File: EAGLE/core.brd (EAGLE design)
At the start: 20.3 x 33 mm, 46 parts, among them Q1 MMDT3904, U1 MIC5219, U3 STM32F10XCXT6, U4 SST25VF040B-50-4I-S2AF, X1 USBUSB-MICROB-ALIGN, Y1 8Mhz

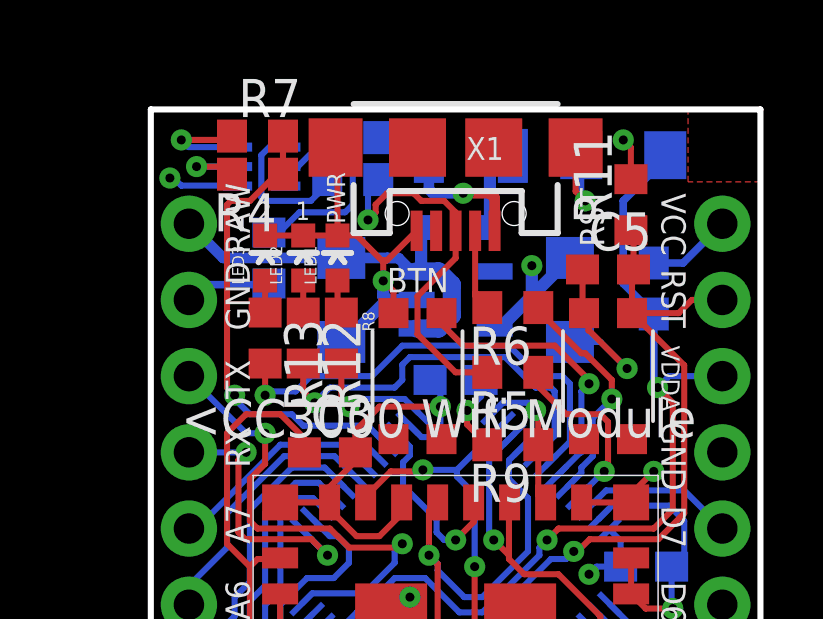
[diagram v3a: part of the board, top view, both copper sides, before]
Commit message: Renumbered parts
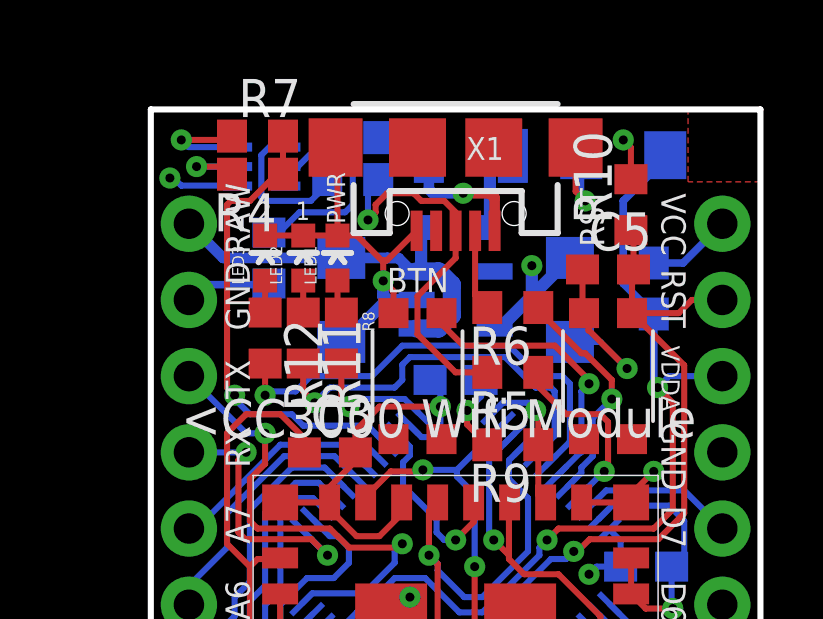
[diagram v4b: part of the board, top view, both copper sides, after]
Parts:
- removed R14: 1K, rcl:R0603
- added R10: 10K, rcl:R0603
- R11: value 10K -> 1K
- moved R13 18.7 mm to (9.65, 7.62), flipped to the bottom
- moved R11 11.8 mm to (5.08, 25.4), turned to 270 degrees
- moved R12 1.27 mm to (3.81, 25.4)
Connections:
- net !RST: now also R10.1; no longer R11.1
- net +3V3: now also R10.2, R13.2; no longer R11.2, R14.2
- net LED1: now also R11.2; no longer R12.2
- net LED2: now also R12.2; no longer R13.2
- net MEM_CS: now also R13.1; no longer R14.1
- net N$10: now also R12.1; no longer R13.1
- net N$2: now also R11.1; no longer R12.1
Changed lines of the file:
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@@
 </element>
 <element name="RESET" library="okie" package="PUSHBUTTON-KMR241GLFS" value="KMR211GLFS" x="15.24" y="24.13" smashed="yes" rot="R90"/>
-<element name="R11" library="rcl" package="R0603" value="10K" x="16.002" y="29.845" smashed="yes" rot="R90">
+<element name="R10" library="rcl" package="R0603" value="10K" x="16.002" y="29.845" smashed="yes" rot="R90">
 <attribute name="NAME" x="15.367" y="29.21" size="1.27" layer="25" rot="R90"/>
 <attribute name="VALUE" x="15.494" y="31.369" size="0.6096" layer="27"/>
 </element>
 <element name="BTN" library="okie" package="PUSHBUTTON-KMR241GLFS" value="KMR211GLFS" x="8.89" y="24.13" smashed="yes" rot="R90"/>
-<element name="R13" library="rcl" package="R0603" value="1K" x="3.81" y="25.4" smashed="yes" rot="R270">
+<element name="R12" library="rcl" package="R0603" value="1K" x="3.81" y="25.4" smashed="yes" rot="R270">
 <attribute name="NAME" x="4.445" y="26.035" size="1.27" layer="25" rot="R270"/>
 <attribute name="VALUE" x="3.302" y="23.368" size="0.6096" layer="27"/>
@@
 <attribute name="VALUE" x="5.9055" y="28.448" size="0.4064" layer="27" rot="R90"/>
 </element>
-<element name="R12" library="rcl" package="R0603" value="1K" x="5.08" y="25.4" smashed="yes" rot="R270">
+<element name="R11" library="rcl" package="R0603" value="1K" x="5.08" y="25.4" smashed="yes" rot="R270">
 <attribute name="NAME" x="5.715" y="26.035" size="1.27" layer="25" rot="R270"/>
 <attribute name="VALUE" x="4.572" y="23.368" size="0.6096" layer="27"/>
@@
 </element>
 <element name="Q1" library="SparkFun-DiscreteSemi" package="SOT363" value="MMDT3904" x="3.683" y="31.115" smashed="yes" rot="MR90"/>
-<element name="R14" library="rcl" package="R0603" value="1K" x="9.652" y="7.62" smashed="yes" rot="MR270">
+<element name="R13" library="rcl" package="R0603" value="1K" x="9.652" y="7.62" smashed="yes" rot="MR270">
 <attribute name="NAME" x="9.017" y="8.255" size="1.27" layer="26" rot="MR270"/>
 <attribute name="VALUE" x="10.16" y="9.144" size="0.6096" layer="28" rot="MR0"/>
@@
 <contactref element="R8" pad="2"/>
 <contactref element="C2" pad="A"/>
-<contactref element="R11" pad="2"/>
+<contactref element="R10" pad="2"/>
 <contactref element="U4" pad="8"/>
 <contactref element="JP2" pad="1"/>
@@
 <contactref element="C7" pad="1"/>
 <contactref element="Q1" pad="3"/>
-<contactref element="R14" pad="2"/>
+<contactref element="R13" pad="2"/>
 <polygon width="0.2032" layer="15" isolate="0.2032">
 <vertex x="0" y="33.02"/>
@@
 <contactref element="U3" pad="7"/>
 <contactref element="RESET" pad="P$2"/>
-<contactref element="R11" pad="1"/>
+<contactref element="R10" pad="1"/>
 <contactref element="JP2" pad="2"/>
 <wire x1="18.034" y1="26.67" x2="19.05" y2="26.67" width="0.2032" layer="1"/>
@@
 </signal>
 <signal name="N$2">
-<contactref element="R12" pad="1"/>
+<contactref element="R11" pad="1"/>
 <contactref element="LED2" pad="A"/>
 <wire x1="5.08" y1="26.25" x2="5.08" y2="27.317" width="0.2032" layer="1"/>
 </signal>
 <signal name="N$10">
-<contactref element="R13" pad="1"/>
+<contactref element="R12" pad="1"/>
 <contactref element="LED3" pad="A"/>
 <wire x1="3.81" y1="26.25" x2="3.81" y2="27.317" width="0.2032" layer="1"/>
@@
 <contactref element="U4" pad="1"/>
 <contactref element="U3" pad="46"/>
-<contactref element="R14" pad="1"/>
+<contactref element="R13" pad="1"/>
 <wire x1="11.303" y1="10.2616" x2="11.303" y2="9.271" width="0.2032" layer="16"/>
 <wire x1="11.303" y1="9.271" x2="10.502" y2="8.47" width="0.2032" layer="16"/>
@@
 <signal name="LED1">
 <contactref element="U3" pad="29"/>
-<contactref element="R12" pad="2"/>
+<contactref element="R11" pad="2"/>
 <wire x1="12.811653125" y1="21.492309375" x2="13.462" y2="22.14265625" width="0.2032" layer="16"/>
 <wire x1="13.462" y1="22.14265625" x2="13.462" y2="23.622" width="0.2032" layer="16"/>
@@
 <signal name="LED2">
 <contactref element="U3" pad="30"/>
-<contactref element="R13" pad="2"/>
+<contactref element="R12" pad="2"/>
 <wire x1="7.366" y1="24.13" x2="5.334" y2="24.13" width="0.2032" layer="16"/>
 <wire x1="13.16520625" y1="21.13875625" x2="13.97" y2="21.94355" width="0.2032" layer="16"/>

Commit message: Updated assembly sheets to v0.1.0
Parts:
- X1: value USBUSB-MICROB-ALIGN -> USB-MICROB
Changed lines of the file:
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@@
 <setting verticaltext="up"/>
 </settings>
-<grid distance="5" unitdist="mil" unit="mil" style="lines" multiple="1" display="yes" altdistance="0.005" altunitdist="inch" altunit="inch"/>
+<grid distance="0.001" unitdist="inch" unit="inch" style="lines" multiple="1" display="yes" altdistance="0.005" altunitdist="inch" altunit="inch"/>
 <layers>
-<layer number="1" name="Top" color="4" fill="1" visible="yes" active="yes"/>
+<layer number="1" name="Top" color="4" fill="1" visible="no" active="yes"/>
 <layer number="2" name="$GND" color="13" fill="1" visible="no" active="yes"/>
 <layer number="3" name="Route3" color="4" fill="3" visible="no" active="no"/>
@@
 <layer number="14" name="Route14" color="1" fill="6" visible="no" active="no"/>
 <layer number="15" name="$+3V3" color="11" fill="1" visible="no" active="yes"/>
-<layer number="16" name="Bottom" color="1" fill="1" visible="yes" active="yes"/>
+<layer number="16" name="Bottom" color="1" fill="1" visible="no" active="yes"/>
 <layer number="17" name="Pads" color="2" fill="1" visible="yes" active="yes"/>
-<layer number="18" name="Vias" color="2" fill="1" visible="yes" active="yes"/>
-<layer number="19" name="Unrouted" color="6" fill="1" visible="yes" active="yes"/>
+<layer number="18" name="Vias" color="2" fill="1" visible="no" active="yes"/>
+<layer number="19" name="Unrouted" color="6" fill="1" visible="no" active="yes"/>
 <layer number="20" name="Dimension" color="6" fill="1" visible="yes" active="yes"/>
 <layer number="21" name="tPlace" color="16" fill="1" visible="no" active="yes"/>
 <layer number="22" name="bPlace" color="14" fill="1" visible="yes" active="yes"/>
-<layer number="23" name="tOrigins" color="15" fill="1" visible="yes" active="yes"/>
+<layer number="23" name="tOrigins" color="15" fill="1" visible="no" active="yes"/>
 <layer number="24" name="bOrigins" color="15" fill="1" visible="yes" active="yes"/>
 <layer number="25" name="tNames" color="7" fill="1" visible="no" active="yes"/>
 <layer number="26" name="bNames" color="7" fill="1" visible="no" active="yes"/>
 <layer number="27" name="tValues" color="7" fill="1" visible="no" active="yes"/>
-<layer number="28" name="bValues" color="7" fill="1" visible="no" active="yes"/>
+<layer number="28" name="bValues" color="7" fill="1" visible="yes" active="yes"/>
 <layer number="29" name="tStop" color="7" fill="3" visible="no" active="yes"/>
 <layer number="30" name="bStop" color="7" fill="6" visible="no" active="yes"/>
 <layer number="31" name="tCream" color="7" fill="4" visible="no" active="yes"/>
-<layer number="32" name="bCream" color="7" fill="5" visible="no" active="yes"/>
+<layer number="32" name="bCream" color="7" fill="5" visible="yes" active="yes"/>
 <layer number="33" name="tFinish" color="6" fill="3" visible="no" active="yes"/>
 <layer number="34" name="bFinish" color="6" fill="6" visible="no" active="yes"/>
@@
 <layer number="49" name="Reference" color="7" fill="1" visible="no" active="yes"/>
 <layer number="50" name="dxf" color="7" fill="1" visible="no" active="yes"/>
-<layer number="51" name="tDocu" color="6" fill="1" visible="yes" active="yes"/>
-<layer number="52" name="bDocu" color="7" fill="1" visible="no" active="yes"/>
+<layer number="51" name="tDocu" color="6" fill="1" visible="no" active="yes"/>
+<layer number="52" name="bDocu" color="7" fill="1" visible="yes" active="yes"/>
 <layer number="53" name="tGND_GNDA" color="7" fill="9" visible="no" active="no"/>
 <layer number="54" name="bGND_GNDA" color="1" fill="9" visible="no" active="no"/>
@@
 <attribute name="VALUE" x="11.557" y="27.051" size="0.6096" layer="27"/>
 </element>
-<element name="X1" library="Spark" package="USB-MICROB-ALIGN" value="USBUSB-MICROB-ALIGN" x="10.16" y="31.75" smashed="yes" rot="R180">
+<element name="X1" library="Spark" package="USB-MICROB-ALIGN" value="USB-MICROB" x="10.16" y="31.75" smashed="yes" rot="R180">
 <attribute name="NAME" x="11.76" y="32.1" size="0.762" layer="25" rot="R180"/>
-<attribute name="VALUE" x="7.62" y="34.671" size="0.6096" layer="27"/>
+<attribute name="VALUE" x="7.366" y="34.671" size="0.6096" layer="27"/>
 </element>
 <element name="F1" library="SparkFun" package="PTC-1206" value="500mA" x="10.668" y="31.4706" smashed="yes" rot="MR180">
@@
 <element name="R1" library="rcl" package="R0603" value="10K" x="6.731" y="32.0802" smashed="yes" rot="MR180">
 <attribute name="NAME" x="6.096" y="31.4452" size="1.27" layer="26" rot="MR180"/>
-<attribute name="VALUE" x="7.239" y="31.0642" size="0.4064" layer="28" rot="MR0"/>
+<attribute name="VALUE" x="7.2644" y="31.2166" size="0.4064" layer="28" rot="MR0"/>
 </element>
 <element name="R3" library="rcl" package="R0603" value="1K5" x="6.731" y="30.6832" smashed="yes" rot="MR0">
 <attribute name="NAME" x="7.366" y="31.3182" size="1.27" layer="26" rot="MR0"/>
-<attribute name="VALUE" x="7.239" y="31.3182" size="0.4064" layer="28" rot="MR0"/>
+<attribute name="VALUE" x="7.1882" y="29.6418" size="0.4064" layer="28" rot="MR0"/>
 </element>
 <element name="C7" library="rcl" package="C0603" value="100nF" x="10.16" y="24.003" smashed="yes" rot="MR0">
@@
 <element name="L2" library="SparkFun-Passives" package="0603" value="Bead" x="16.764" y="27.051" smashed="yes" rot="MR270">
 <attribute name="NAME" x="16.002" y="27.94" size="0.4064" layer="26" font="vector" rot="MR270"/>
-<attribute name="VALUE" x="17.526" y="25.146" size="0.4064" layer="28" font="vector" rot="MR0"/>
+<attribute name="VALUE" x="17.4498" y="25.146" size="0.4064" layer="28" font="vector" rot="MR0"/>
 </element>
 <element name="R4" library="rcl" package="R0603" value="1K" x="3.556" y="30.861" smashed="yes" rot="R180">
@@
 </signal>
 </signals>
-<errors>
-</errors>
 </board>
 </drawing>

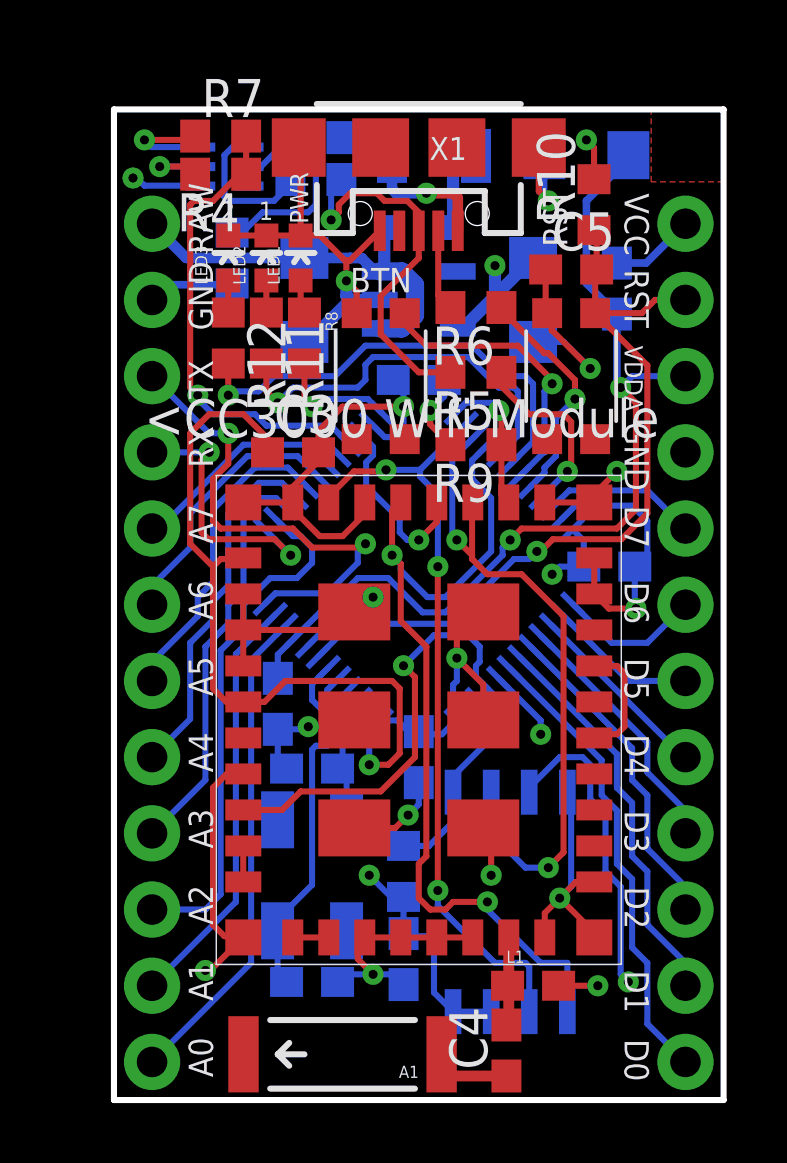
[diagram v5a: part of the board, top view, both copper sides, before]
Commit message: WIP for Issue #5, #7, #8, #9
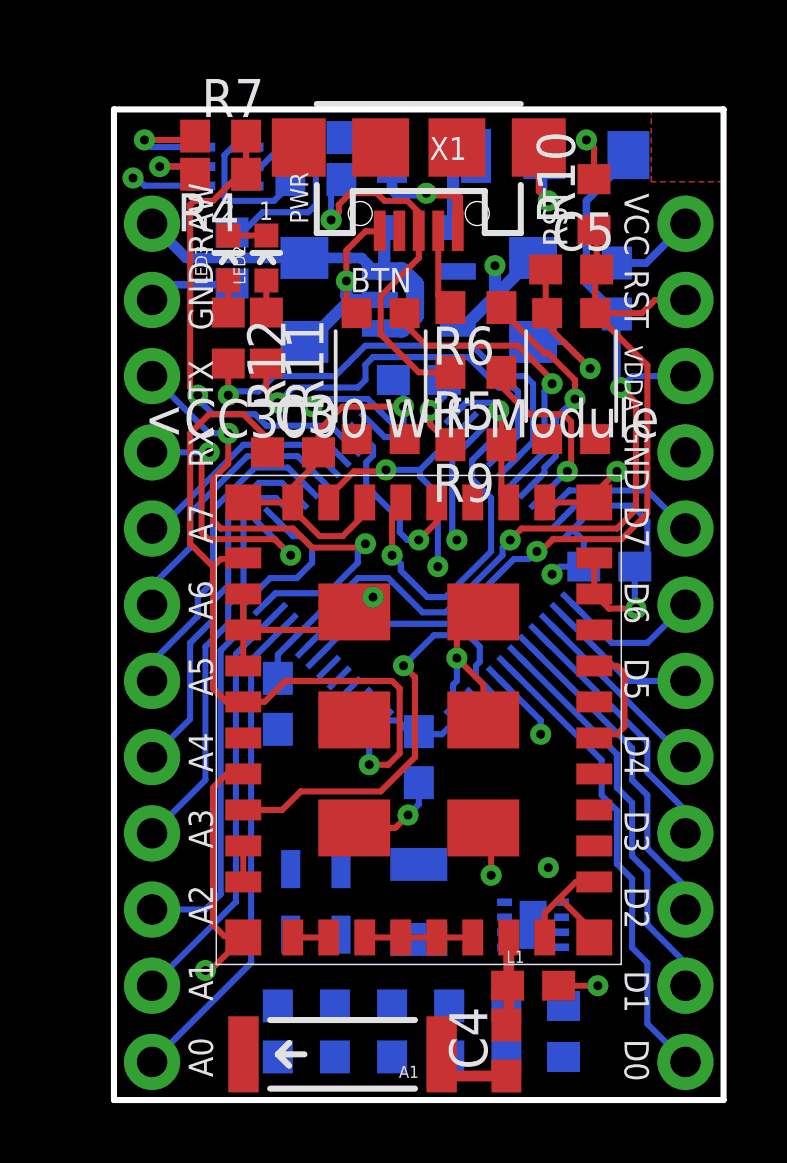
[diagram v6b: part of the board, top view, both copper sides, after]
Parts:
- removed LED1: Red, SparkFun:LED-0603
- removed R8: 1K, rcl:R0603
- added C14, C15: 12.5pF, rcl:C0603
- added Y2: 32Khz, Spark:FC135
- U4: value SST25VF040B-50-4I-S2AF -> SST25VF040B-Q; device Silicon_Storage_Tech_By_element14_Batch_1:SOIC127P790X216-8N -> Spark:WSON-8-PAD
- Y1: device SparkFun:CRYSTAL-SMD-5X3 -> Spark:OSC3.2X.2.5
- moved C9 8.80 mm to (7.37, 2.29), turned to 270 degrees
- moved R13 7.54 mm to (15.0, 2.29), turned to 90 degrees
- moved C6 4.19 mm to (13.1, 2.29)
- moved C8 2.01 mm to (5.46, 2.29), turned to 270 degrees
- moved U4 1.08 mm to (14.0, 5.84)
- moved Y1 0.90 mm to (6.73, 6.60)
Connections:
- removed net N$38: LED1.A, R8.1
- removed net OSC1: C8.1, U3.6, Y1.3
- removed net OSC2: C9.1, U3.5, Y1.1
- new net OSC32_IN: C15.1, U3.3, Y2.X1
- new net OSC32_OUT: C14.1, U3.4, Y2.X2
- new net OSC_IN: C9.1, U3.5, Y1.P$1
- new net OSC_OUT: C8.1, U3.6, Y1.P$3
- net +3V3: no longer R8.2
- net GND: now also C14.2, C15.2; no longer LED1.C
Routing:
- net SPI_MOSI: track 30.4 -> 10.6 mm, vias 2 -> 1
- net +3V3: track 69.0 -> 49.3 mm, vias 9 -> 7
- net SPI_MISO: track 23.4 -> 4.63 mm
- net GND: track 112.6 -> 94.8 mm, vias 17 -> 14
- net SPI_SCK: track 26.4 -> 9.71 mm, vias 3 -> 2
- net OSC1: track 12.1 -> 0.00 mm
- net MEM_CS: track 6.79 -> 0.00 mm
- net OSC2: track 5.29 -> 0.00 mm
- net N$38: track 1.12 -> 0.00 mm

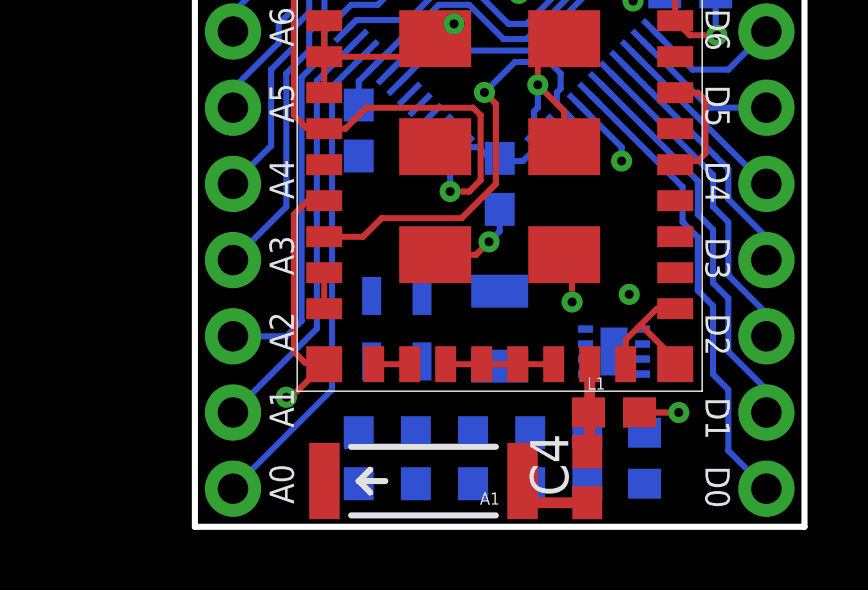
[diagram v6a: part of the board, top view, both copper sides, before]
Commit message: Moved crystals and capacitors away from RF area
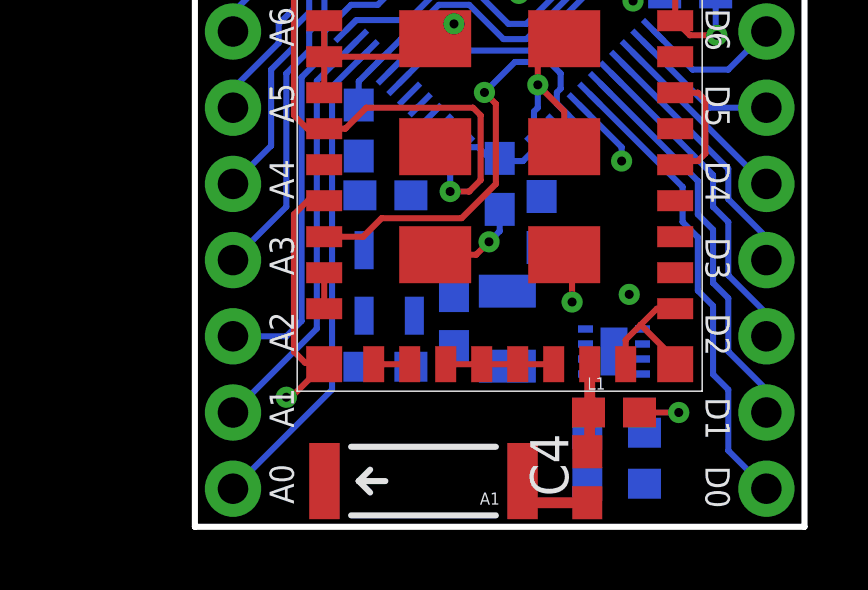
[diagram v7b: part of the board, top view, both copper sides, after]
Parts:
- moved C8 8.81 mm to (6.35, 11.0), turned to 0 degrees
- moved C14 8.20 mm to (11.6, 10.2), turned to 90 degrees
- moved C15 5.23 mm to (8.64, 6.86), turned to 90 degrees
- moved C9 3.21 mm to (6.35, 5.33), turned to 0 degrees
- moved Y1 1.55 mm to (6.48, 8.13)
- moved Y2 0.25 mm to (10.4, 6.60), turned to 90 degrees
